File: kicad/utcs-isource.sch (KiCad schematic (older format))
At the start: 19 parts

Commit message: Place and Route Complete, finishing touches
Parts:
- removed J?: Conn_01x05, symbol Conn_01x05
- added J1: Conn_01x06, footprints:PCB_HDR_100MIL_1X6_MOL-0705530005, symbol Conn_01x06
- added TP1: +5V, Pin_Headers:Pin_Header_Straight_1x01_Pitch2.54mm, symbol TEST_1P
- added TP15: AVSS, Pin_Headers:Pin_Header_Straight_1x01_Pitch2.54mm, symbol TEST_1P
- added TP16: INST_REF, Pin_Headers:Pin_Header_Straight_1x01_Pitch2.54mm, symbol TEST_1P
- added TP17: AVDD, Pin_Headers:Pin_Header_Straight_1x01_Pitch2.54mm, symbol TEST_1P
- added TP18: INSTR_OUT, Pin_Headers:Pin_Header_Straight_1x01_Pitch2.54mm, symbol TEST_1P
- added TP2: ~CS, Pin_Headers:Pin_Header_Straight_1x01_Pitch2.54mm, symbol TEST_1P
- added TP22, TP23: IOUT, Pin_Headers:Pin_Header_Straight_1x01_Pitch2.54mm, symbol TEST_1P
- added TP25: IRET, Pin_Headers:Pin_Header_Straight_1x01_Pitch2.54mm, symbol TEST_1P
- added TP26: GND, Pin_Headers:Pin_Header_Straight_1x01_Pitch2.54mm, symbol TEST_1P
- added TP3: MOSI, Pin_Headers:Pin_Header_Straight_1x01_Pitch2.54mm, symbol TEST_1P
- added TP4: SCLK, Pin_Headers:Pin_Header_Straight_1x01_Pitch2.54mm, symbol TEST_1P
- added TP6: AGND, Pin_Headers:Pin_Header_Straight_1x01_Pitch2.54mm, symbol TEST_1P
- added TP7: DAC_REF, Pin_Headers:Pin_Header_Straight_1x01_Pitch2.54mm, symbol TEST_1P
- added TP9: DAC_OUT, Pin_Headers:Pin_Header_Straight_1x01_Pitch2.54mm, symbol TEST_1P
- C1, C3, C6, C7, C8: renamed from C?; footprint (none) -> Capacitors_SMD:C_0805_HandSoldering
- C2, C4: renamed from C?; footprint (none) -> Capacitors_SMD:C_1206_HandSoldering
- C5: renamed from C?; value C -> 10n; footprint (none) -> Capacitors_SMD:C_0805_HandSoldering
- C9: renamed from C?; value C -> 100n; footprint (none) -> Capacitors_SMD:C_0805_HandSoldering
- J2: renamed from J?; footprint (none) -> footprints:PCB_TB_1X3_PHC-1790296
- P1: renamed from P?; footprint (none) -> footprints:PCB_TB_1X2_PHC-1790283
- R1: renamed from R?; footprint (none) -> Resistors_SMD:R_0805_HandSoldering
- R2, R3, R4: renamed from R?; footprint (none) -> Resistors_SMD:R_1206_HandSoldering
- U1: renamed from U?; footprint (none) -> TO_SOT_Packages_SMD:SOT-23-8_Handsoldering
- U2, U3: renamed from U?; footprint (none) -> SMD_Packages:SOIC-8-N
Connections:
- net +5V: now also J1.6 (Pin_6), TP1.1
- net AVDD: now also TP17.1
- net AVSS: now also TP15.1
- net GND: now also J1.1 (Pin_1), TP25.1, TP26.1, TP6.1
- net IOUT: now also TP22.1, TP23.1
- net at C5.1, U1.2 (VREF): now also U2.4 (+), TP7.1; no longer U2.1 (-)
- net at U1.3 (VFB), U1.4 (VOUT): now also U2.1 (-), TP9.1; no longer U2.4 (+)
- net at U2.6 (REF), U3.2 (-), U3.6 (OUT): now also TP16.1
- net at R2.2, R3.2, R4.2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: now also TP18.1
- net at U1.5 (~CS): now also J1.2 (Pin_2), TP2.1
- net at U1.6 (SCLK): now also J1.3 (Pin_3), TP4.1
- net SPI_MOSI: now reaches U1.7 (MOSI)
- net SPI_MOSI: now also J1.4 (Pin_4), TP3.1
- no-connect marks 0 -> 2

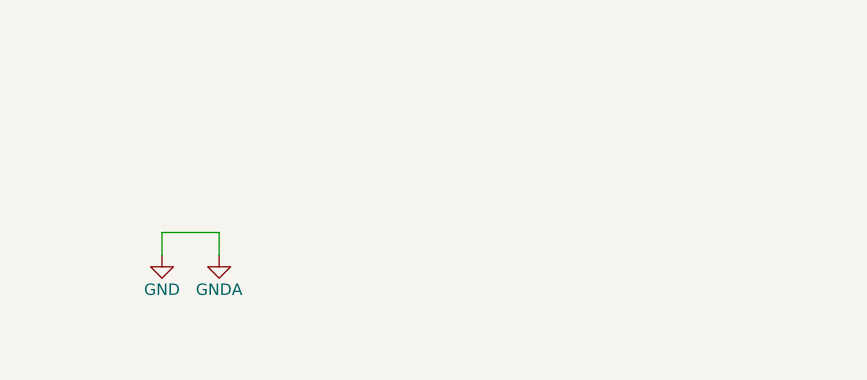
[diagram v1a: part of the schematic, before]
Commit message: Updated to double sided plating for through hole components
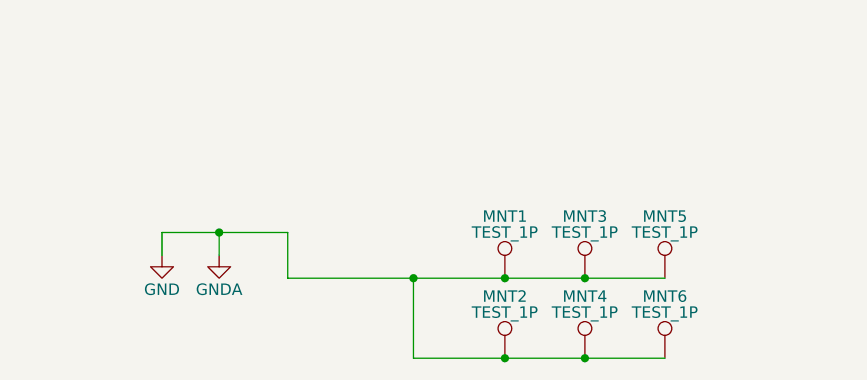
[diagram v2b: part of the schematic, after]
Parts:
- added MNT1, MNT2, MNT3, MNT4, MNT5, MNT6: TEST_1P, Mounting_Holes:MountingHole_4.5mm_Pad, symbol TEST_1P
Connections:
- net GND: now also MNT1.1, MNT2.1, MNT3.1, MNT4.1, MNT5.1, MNT6.1
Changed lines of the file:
@@
 	2450 6050 2450 5950
 Wire Wire Line
-	2450 5950 2700 5950
+	2450 5950 3000 5950
 Wire Wire Line
 	2700 5950 2700 6050
@@
 	6950 4000 7050 4000
 NoConn ~ 6250 500
+$Comp
+L TEST_1P MNT1
+U 1 1 5A440FB6
+P 3950 6150
+F 0 "MNT1" H 3950 6420 50  0000 C CNN
+F 1 "TEST_1P" H 3950 6350 50  0000 C CNN
+F 2 "Mounting_Holes:MountingHole_4.5mm_Pad" H 4150 6150 50  0001 C CNN
+F 3 "" H 4150 6150 50  0001 C CNN
+	1    3950 6150
+	1    0    0    -1
+$EndComp
+$Comp
+L TEST_1P MNT3
+U 1 1 5A4416B5
+P 4300 6150
+F 0 "MNT3" H 4300 6420 50  0000 C CNN
+F 1 "TEST_1P" H 4300 6350 50  0000 C CNN
+F 2 "Mounting_Holes:MountingHole_4.5mm_Pad" H 4500 6150 50  0001 C CNN
+F 3 "" H 4500 6150 50  0001 C CNN
+	1    4300 6150
+	1    0    0    -1
+$EndComp
+$Comp
+L TEST_1P MNT5
+U 1 1 5A44173F
+P 4650 6150
+F 0 "MNT5" H 4650 6420 50  0000 C CNN
+F 1 "TEST_1P" H 4650 6350 50  0000 C CNN
+F 2 "Mounting_Holes:MountingHole_4.5mm_Pad" H 4850 6150 50  0001 C CNN
+F 3 "" H 4850 6150 50  0001 C CNN
+	1    4650 6150
+	1    0    0    -1
+$EndComp
+$Comp
+L TEST_1P MNT2
+U 1 1 5A4417D0
+P 3950 6500
+F 0 "MNT2" H 3950 6770 50  0000 C CNN
+F 1 "TEST_1P" H 3950 6700 50  0000 C CNN
+F 2 "Mounting_Holes:MountingHole_4.5mm_Pad" H 4150 6500 50  0001 C CNN
+F 3 "" H 4150 6500 50  0001 C CNN
+	1    3950 6500
+	1    0    0    -1
+$EndComp
+$Comp
+L TEST_1P MNT4
+U 1 1 5A44188E
+P 4300 6500
+F 0 "MNT4" H 4300 6770 50  0000 C CNN
+F 1 "TEST_1P" H 4300 6700 50  0000 C CNN
+F 2 "Mounting_Holes:MountingHole_4.5mm_Pad" H 4500 6500 50  0001 C CNN
+F 3 "" H 4500 6500 50  0001 C CNN
+	1    4300 6500
+	1    0    0    -1
+$EndComp
+$Comp
+L TEST_1P MNT6
+U 1 1 5A44191F
+P 4650 6500
+F 0 "MNT6" H 4650 6770 50  0000 C CNN
+F 1 "TEST_1P" H 4650 6700 50  0000 C CNN
+F 2 "Mounting_Holes:MountingHole_4.5mm_Pad" H 4850 6500 50  0001 C CNN
+F 3 "" H 4850 6500 50  0001 C CNN
+	1    4650 6500
+	1    0    0    -1
+$EndComp
+Wire Wire Line
+	3000 6150 4650 6150
+Connection ~ 4300 6150
+Wire Wire Line
+	3550 6150 3550 6500
+Wire Wire Line
+	3550 6500 4650 6500
+Connection ~ 3950 6150
+Connection ~ 3950 6500
+Connection ~ 4300 6500
+Wire Wire Line
+	3000 5950 3000 6150
+Connection ~ 2700 5950
+Connection ~ 3550 6150
 $EndSCHEMATC
